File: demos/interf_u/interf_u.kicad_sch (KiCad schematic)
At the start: 24 parts, among them P1 DB25FEMELLE, U1 74LS245, U2 74LS688, U3 74LS541, U5 628128, U8 EP600, U9 4003APG120, X1 8MHz

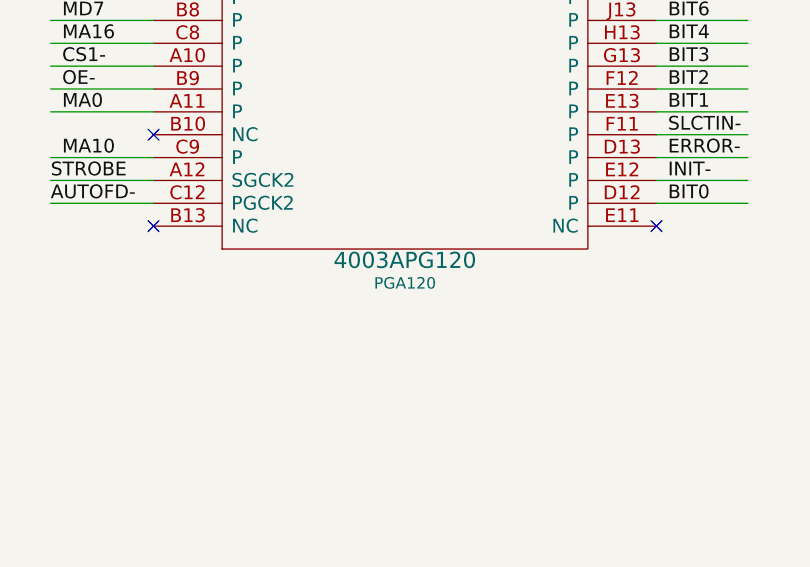
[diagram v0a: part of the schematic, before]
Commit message: feat: update kicad to 9.0.0+dfsg-1
Signed-off-by: lhdjply <lhdjply@126.com>
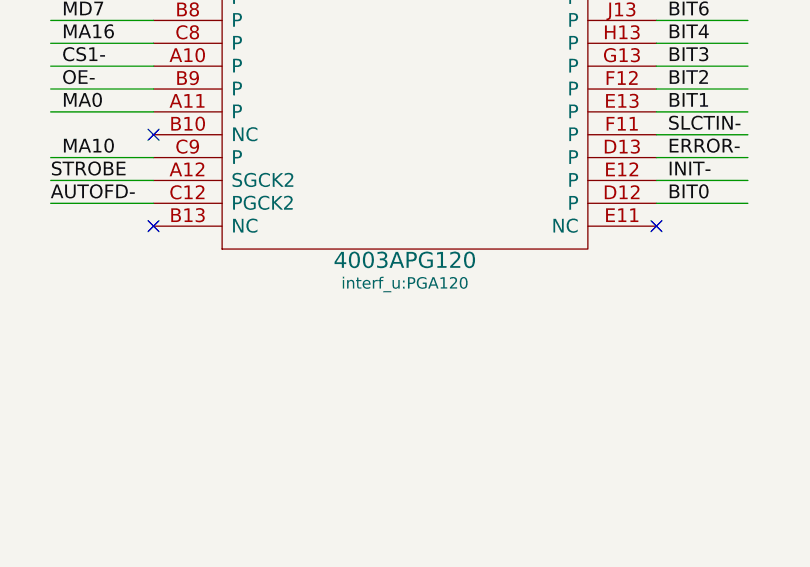
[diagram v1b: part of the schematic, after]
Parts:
- BUS1: symbol interf_u_schlib:Bus_ISA_8bit -> interf_u:Bus_ISA_8bit
- C1, C4, C5, C6: symbol interf_u_schlib:CP -> interf_u:CP
- C2, C3: symbol interf_u_schlib:C -> interf_u:C
- D1, D2: symbol interf_u_schlib:LED -> interf_u:LED
- JP1: symbol interf_u_schlib:Conn_02x08_Odd_Even -> interf_u:Conn_02x08_Odd_Even
- P1: symbol interf_u_schlib:DB25_Female -> interf_u:DB25_Female
- R1, R2, R3, R4, R5: symbol interf_u_schlib:R -> interf_u:R
- RR1: symbol interf_u_schlib:RR9 -> interf_u:RR9
- U1: symbol interf_u_schlib:74LS245 -> interf_u:74LS245
- U2: symbol interf_u_schlib:74LS688 -> interf_u:74LS688
- U3: symbol interf_u_schlib:74LS541 -> interf_u:74LS541
- U5: symbol interf_u_schlib:628128 -> interf_u:628128
- U8: symbol interf_u_schlib:EP600 -> interf_u:EP600
- U9: footprint PGA120 -> interf_u:PGA120; symbol interf_u_schlib:4003APG120 -> interf_u:4003APG120
- X1: symbol interf_u_schlib:Crystal -> interf_u:Crystal
